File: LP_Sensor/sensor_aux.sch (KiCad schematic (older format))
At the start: 2 parts

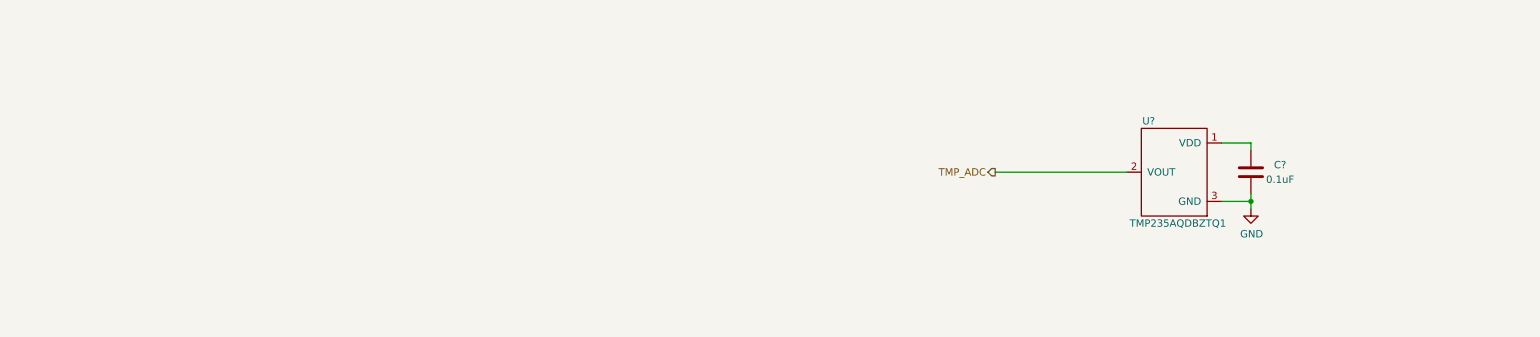
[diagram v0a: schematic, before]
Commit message: Added IMU to Sensor page.
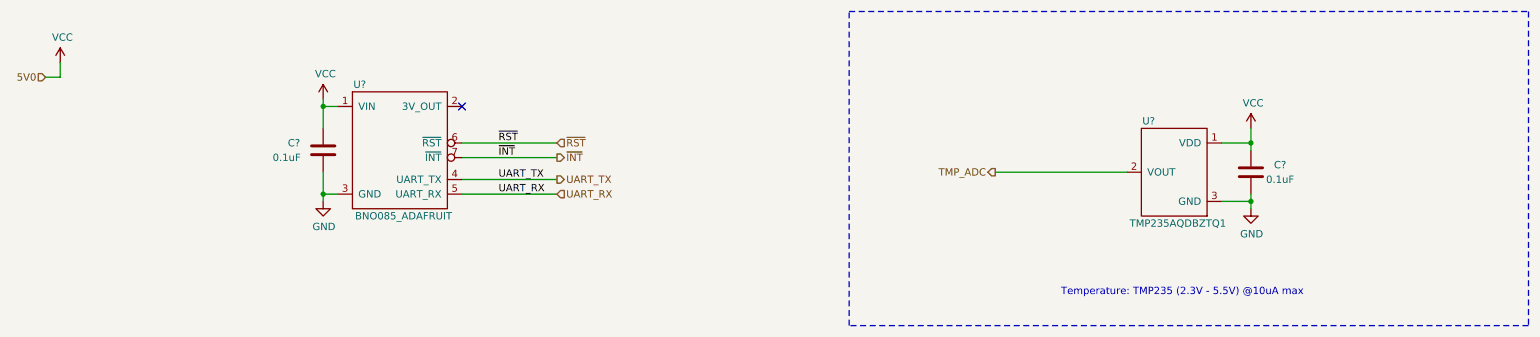
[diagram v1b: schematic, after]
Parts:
- added C?: 0.1uF, symbol Device:C
- added U?: BNO085_ADAFRUIT, symbol ritchie0:BNO085_ADAFRUIT
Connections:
- net GND: now also C?.2, U?.3 (GND)
- net VCC: now reaches C?.1, U?.1 (VDD)
- net VCC: now also C?.1, U?.1 (VIN)
- new net UART_RX: U?.5 (UART_RX)
- new net UART_TX: U?.4 (UART_TX)
- new net ~INT: U?.7 (~INT)
- new net ~RST: U?.6 (~RST)
- no-connect marks 0 -> 1
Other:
- note added: "Temperature: TMP235 (2.3V - 5.5V) @10uA max"
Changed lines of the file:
@@
 $Descr A4 11693 8268
 encoding utf-8
-Sheet 3 5
+Sheet 5 5
 Title ""
 Date ""
@@
 Wire Wire Line
 	8400 1650 7500 1650
+Wire Notes Line
+	6500 2700 6500 550
+Wire Notes Line
+	6500 550  11150 550
+Wire Notes Line
+	11150 550  11150 2700
+Wire Notes Line
+	11150 2700 6500 2700
+Text Notes 7950 2500 0    50   ~ 0
+Temperature: TMP235 (2.3V - 5.5V) @10uA max
+Text HLabel 1000 1000 0    50   Input ~ 0
+5V0
+$Comp
+L power:VCC #PWR?
+U 1 1 61442E26
+P 1100 900
+F 0 "#PWR?" H 1100 750 50  0001 C CNN
+F 1 "VCC" H 1115 1073 50  0000 C CNN
+F 2 "" H 1100 900 50  0001 C CNN
+F 3 "" H 1100 900 50  0001 C CNN
+	1    1100 900
+	1    0    0    -1
+$EndComp
+Wire Wire Line
+	1100 900  1100 1000
+Wire Wire Line
+	1100 1000 1000 1000
+$Comp
+L power:VCC #PWR?
+U 1 1 61443E3D
+P 9250 1350
+F 0 "#PWR?" H 9250 1200 50  0001 C CNN
+F 1 "VCC" H 9265 1523 50  0000 C CNN
+F 2 "" H 9250 1350 50  0001 C CNN
+F 3 "" H 9250 1350 50  0001 C CNN
+	1    9250 1350
+	1    0    0    -1
+$EndComp
+Wire Wire Line
+	9250 1350 9250 1450
+Connection ~ 9250 1450
+$Comp
+L ritchie0:BNO085_ADAFRUIT U?
+U 1 1 614483CA
+P 3400 1500
+F 0 "U?" H 3150 1950 50  0000 C CNN
+F 1 "BNO085_ADAFRUIT" H 3450 1050 50  0000 C CNN
+F 2 "" H 3350 1400 50  0001 C CNN
+F 3 "" H 3350 1400 50  0001 C CNN
+	1    3400 1500
+	1    0    0    -1
+$EndComp
+$Comp
+L power:VCC #PWR?
+U 1 1 61449079
+P 2900 1150
+F 0 "#PWR?" H 2900 1000 50  0001 C CNN
+F 1 "VCC" H 2915 1323 50  0000 C CNN
+F 2 "" H 2900 1150 50  0001 C CNN
+F 3 "" H 2900 1150 50  0001 C CNN
+	1    2900 1150
+	1    0    0    -1
+$EndComp
+$Comp
+L power:GND #PWR?
+U 1 1 614496CE
+P 2900 1850
+F 0 "#PWR?" H 2900 1600 50  0001 C CNN
+F 1 "GND" H 2905 1677 50  0000 C CNN
+F 2 "" H 2900 1850 50  0001 C CNN
+F 3 "" H 2900 1850 50  0001 C CNN
+	1    2900 1850
+	1    0    0    -1
+$EndComp
+$Comp
+L Device:C C?
+U 1 1 6144A582
+P 2900 1500
+F 0 "C?" H 2700 1550 50  0000 C CNN
+F 1 "0.1uF" H 2650 1450 50  0000 C CNN
+F 2 "" H 2938 1350 50  0001 C CNN
+F 3 "~" H 2900 1500 50  0001 C CNN
+	1    2900 1500
+	1    0    0    -1
+$EndComp
+Wire Wire Line
+	2900 1150 2900 1200
+Wire Wire Line
+	2900 1650 2900 1800
+Wire Wire Line
+	3000 1800 2900 1800
+Connection ~ 2900 1800
+Wire Wire Line
+	2900 1800 2900 1850
+Wire Wire Line
+	3000 1200 2900 1200
+Connection ~ 2900 1200
+Wire Wire Line
+	2900 1200 2900 1350
+Text HLabel 4500 1700 2    50   Output ~ 0
+UART_TX
+Text HLabel 4500 1800 2    50   Input ~ 0
+UART_RX
+Text HLabel 4500 1550 2    50   Output ~ 0
+~INT
+Text HLabel 4500 1450 2    50   Input ~ 0
+~RST
+NoConn ~ 3850 1200
+Wire Wire Line
+	3850 1700 4500 1700
+Wire Wire Line
+	3850 1800 4500 1800
+Wire Wire Line
+	3850 1550 4500 1550
+Wire Wire Line
+	3850 1450 4500 1450
+Text Label 4100 1800 0    50   ~ 0
+UART_RX
+Text Label 4100 1700 0    50   ~ 0
+UART_TX
+Text Label 4100 1550 0    50   ~ 0
+~INT
+Text Label 4100 1450 0    50   ~ 0
+~RST
 $EndSCHEMATC
